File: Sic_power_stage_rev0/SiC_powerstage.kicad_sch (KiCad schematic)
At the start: 34 parts, among them Q10 NTBG014N120M3P, Q11 NTBG014N120M3P, Q12 NTBG014N120M3P, Q7 NTBG014N120M3P, Q8 NTBG014N120M3P, Q9 NTBG014N120M3P

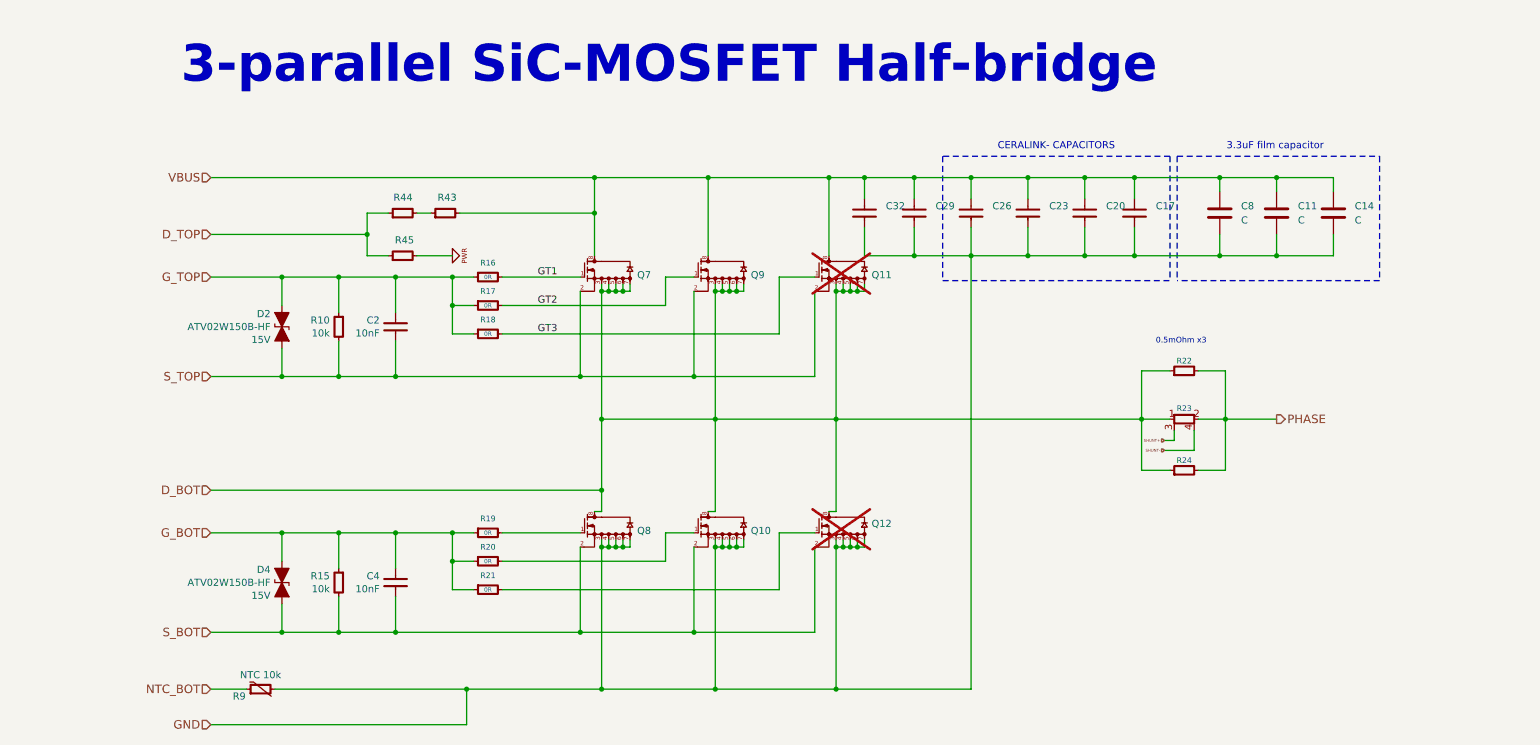
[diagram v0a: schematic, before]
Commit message: Increase clearance between mosfets, Add alternating film capacitor
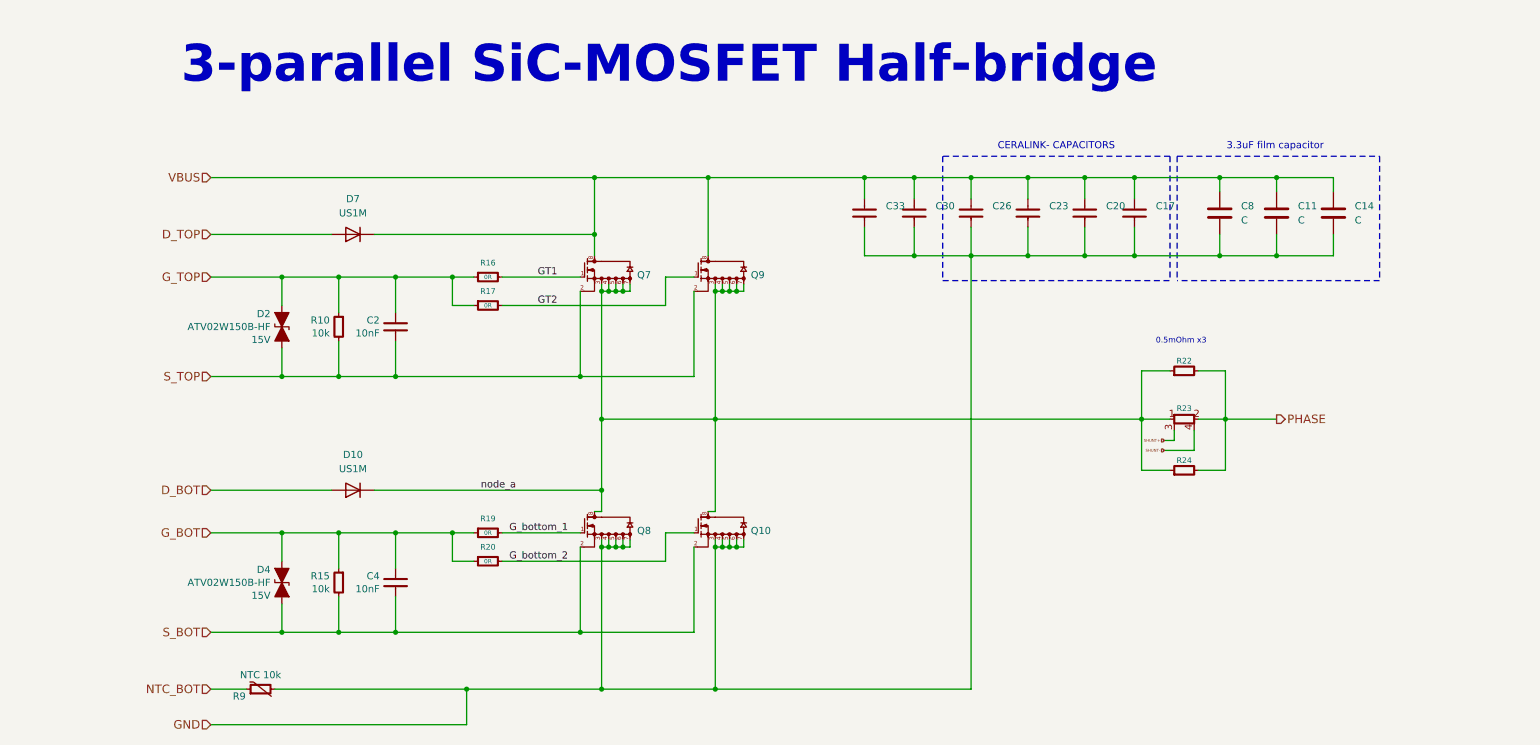
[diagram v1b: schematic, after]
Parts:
- removed Q11, Q12: NTBG014N120M3P, SiC_ONSEMI:D2PAK-7L, symbol SiC_ONSEMI:NTB6014N120M3P
- removed R18, R21: 0R, IPC7351-Nominal:RESC1608X50, symbol pasv-res:R-0603
- removed R43, R44, R45: R-1206, IPC7351-Nominal:RESC3216X60, symbol pasv-res:R-1206
- added D10, D7: US1M, Diode_SMD:D_SMA, symbol Diode:US1M
- renumbered C29 to C30, C32 to C33
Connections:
- net D_BOT: now also D10.2 (A); no longer Q10.8, Q7.3, Q7.4, Q7.5, Q7.6, Q7.7, Q8.8, Q9.3, Q9.4, Q9.5, Q9.6, Q9.7, R22.1, R23.1, R24.1
- net D_TOP: now also D7.2 (A)
- net VBUS: now also D7.1 (K)
- net G_bottom_2: now reaches Q10.1, R20.2
- net G_bottom_1: now reaches Q8.1, R19.2
- new net node_a: D10.1 (K), Q10.8, Q7.3, Q7.4, Q7.5, Q7.6, Q7.7, Q8.8, Q9.3, Q9.4, Q9.5, Q9.6, Q9.7, R22.1, R23.1, R24.1

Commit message: Move leg A to reduce Cu Area
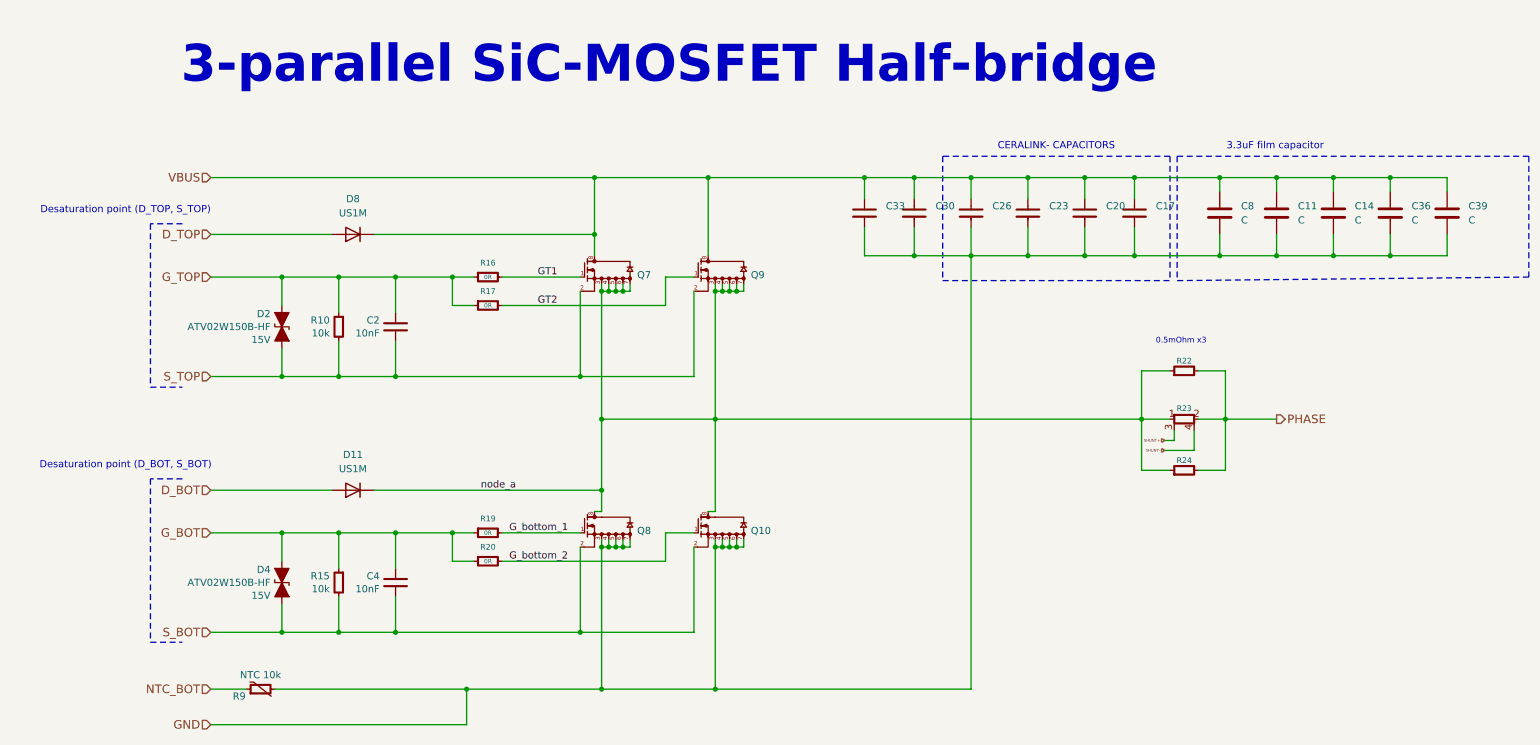
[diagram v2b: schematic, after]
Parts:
- added C36, C39: C, Capacitor_THT:C_Rect_L18.0mm_W9.0mm_P15.00mm_FKS3_FKP3, symbol Device:C
- renumbered D10 to D11, D7 to D8
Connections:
- net GND: now also C36.2, C39.2
- net VBUS: now also C36.1, C39.1
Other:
- note added: "Desaturation point (D_BOT, S_BOT)"
- note added: "Desaturation point (D_TOP, S_TOP)"

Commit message: Define Ceralink capacitor value and qty
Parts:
- C10: renamed from C11; value C -> 5uF; footprint Capacitor_THT:C_Rect_L18.0mm_W9.0mm_P15.00mm_FKS3_FKP3 -> Capacitor_THT:C_Rect_L31.5mm_W11.0mm_P27.50mm_MKS4; BOM (none) -> MKP DC FILTERING - 500VDC, 5UF 1; MFR (none) -> EPCOS - TDK Electronics; MPN (none) -> B32714H5505K000; Voltage (none) -> 500V
- C11: renamed from C14; value C -> 5uF; footprint Capacitor_THT:C_Rect_L18.0mm_W9.0mm_P15.00mm_FKS3_FKP3 -> Capacitor_THT:C_Rect_L31.5mm_W11.0mm_P27.50mm_MKS4; BOM (none) -> MKP DC FILTERING - 500VDC, 5UF 1; MFR (none) -> EPCOS - TDK Electronics; MPN (none) -> B32714H5505K000; Voltage (none) -> 500V
- C12: renamed from C36; value C -> 5uF; footprint Capacitor_THT:C_Rect_L18.0mm_W9.0mm_P15.00mm_FKS3_FKP3 -> Capacitor_THT:C_Rect_L31.5mm_W11.0mm_P27.50mm_MKS4; BOM (none) -> MKP DC FILTERING - 500VDC, 5UF 1; MFR (none) -> EPCOS - TDK Electronics; MPN (none) -> B32714H5505K000; Voltage (none) -> 500V
- C13: renamed from C39; value C -> 5uF; BOM (none) -> MKP DC FILTERING - 500VDC, 5UF 1; MFR (none) -> EPCOS - TDK Electronics; MPN (none) -> B32714H5505K000; Voltage (none) -> 500V
- C3: renamed from C33; value C-2220 -> 0.25uF; BOM (none) -> CERALINK SMD 2220 - 500 V; MFR (none) -> EPCOS - TDK Electronics; MPN (none) -> B58043I5254M052; Volatage (none) -> 500V
- C4: renamed from C30; value C-2220 -> 0.25uF; BOM (none) -> CERALINK SMD 2220 - 500 V; MFR (none) -> EPCOS - TDK Electronics; MPN (none) -> B58043I5254M052; Voltage (none) -> 500V
- C5: renamed from C26; value C-2220 -> 0.25uF; BOM (none) -> CERALINK SMD 2220 - 500 V; MFR (none) -> EPCOS - TDK Electronics; MPN (none) -> B58043I5254M052; Voltage (none) -> 500V
- C6: renamed from C23; value C-2220 -> 0.25uF; BOM (none) -> CERALINK SMD 2220 - 500 V; MFR (none) -> EPCOS - TDK Electronics; MPN (none) -> B58043I5254M052; Voltage (none) -> 500V
- C7: renamed from C20; value C-2220 -> 0.25uF; BOM (none) -> CERALINK SMD 2220 - 500 V; MFR (none) -> EPCOS - TDK Electronics; MPN (none) -> B58043I5254M052; Voltage (none) -> 500V
- C8: renamed from C17; value C-2220 -> 0.25uF; BOM (none) -> CERALINK SMD 2220 - 500 V; MFR (none) -> EPCOS - TDK Electronics; MPN (none) -> B58043I5254M052; Voltage (none) -> 500V
- C9: renamed from C8; value C -> 5uF; footprint Capacitor_THT:C_Rect_L18.0mm_W9.0mm_P15.00mm_FKS3_FKP3 -> Capacitor_THT:C_Rect_L31.5mm_W11.0mm_P27.50mm_MKS4; BOM (none) -> MKP DC FILTERING - 500VDC, 5UF 1; MFR (none) -> EPCOS - TDK Electronics; MPN (none) -> B32714H5505K000; Voltage (none) -> 500V
- Q1: renamed from Q7; footprint SiC_ONSEMI:D2PAK-7L -> Package_TO_SOT_SMD:TO-263-7_TabPin8; BOM (none) -> D2PAK7(TO-263-7L-HV) Silicon Carbide Field Effect Transisto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; LCSC Part # (none) -> C5209029; MFR (none) -> onsemi; MPN (none) -> NTBG014N120M3P
- Q2: renamed from Q8; footprint SiC_ONSEMI:D2PAK-7L -> Package_TO_SOT_SMD:TO-263-7_TabPin8; BOM (none) -> D2PAK7(TO-263-7L-HV) Silicon Carbide Field Effect Transisto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; LCSC Part # (none) -> C5209029; MFR (none) -> onsemi; MPN (none) -> NTBG014N120M3P
- Q3: renamed from Q9; footprint SiC_ONSEMI:D2PAK-7L -> Package_TO_SOT_SMD:TO-263-7_TabPin8; BOM (none) -> D2PAK7(TO-263-7L-HV) Silicon Carbide Field Effect Transisto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; LCSC Part # (none) -> C5209029; MFR (none) -> onsemi; MPN (none) -> NTBG014N120M3P
- Q4: renamed from Q10; footprint SiC_ONSEMI:D2PAK-7L -> Package_TO_SOT_SMD:TO-263-7_TabPin8; BOM (none) -> D2PAK7(TO-263-7L-HV) Silicon Carbide Field Effect Transisto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; LCSC Part # (none) -> C5209029; MFR (none) -> onsemi; MPN (none) -> NTBG014N120M3P
- renumbered C2 to C1, C4 to C2, D2 to D1, D4 to D2, D8 to D3, D11 to D4, R20 to R10, R22 to R11, R23 to R12, R24 to R13, R9 to R4, R10 to R5, R15 to R6, R16 to R7, R17 to R8, R19 to R9
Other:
- note added: "For 5uF rated 500v, rated size: 1.240" L x 0.433" W (31.50mm x 11.00mm)"
- note added: "SiC-MOSFET Half-bridge"
- note removed: "3-parallel SiC-MOSFET Half-bridge"
- moved on the sheet: C10, C11, C12, C13, C3, C5, C6, C7, C8, C9

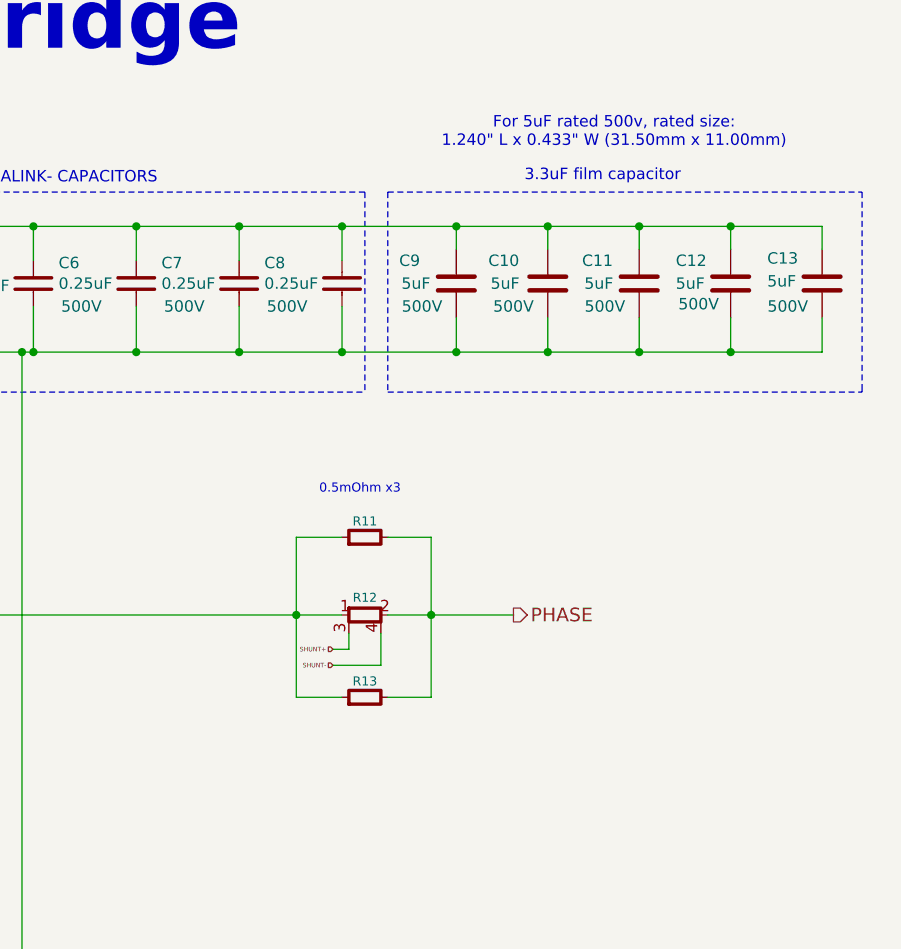
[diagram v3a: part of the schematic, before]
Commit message: Add changes
 - Add DC-LINK capacitor discharge circuit.
 - VBUS resistive divider.
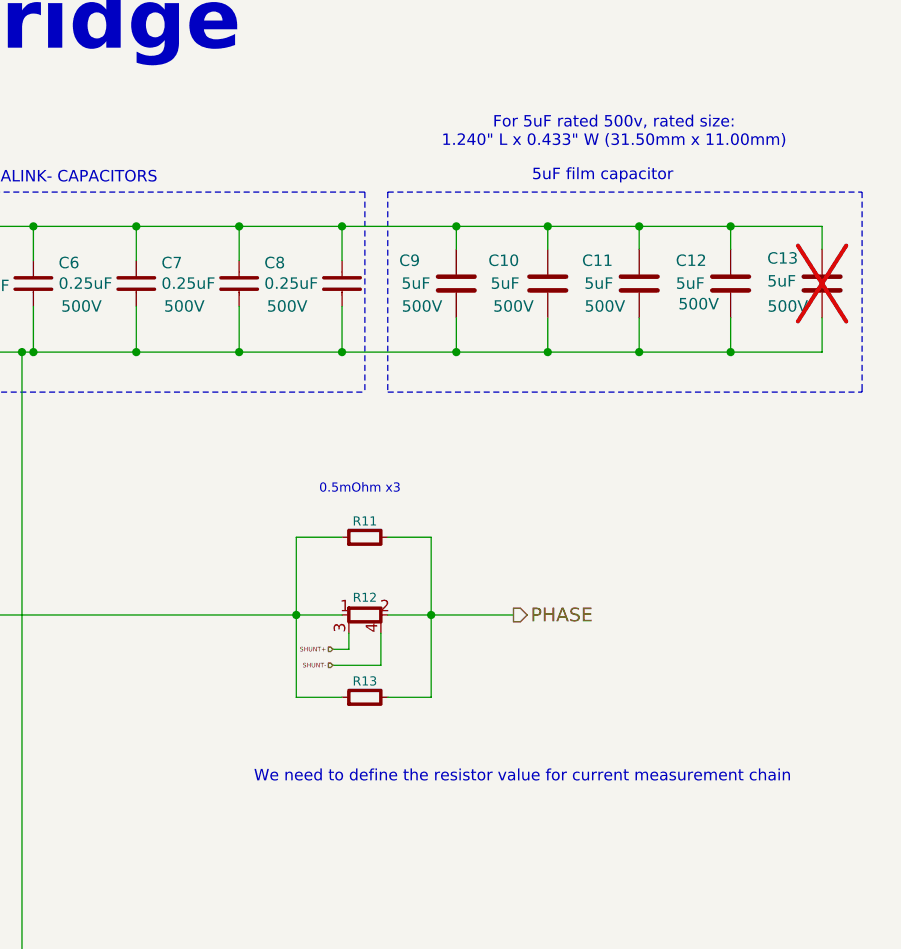
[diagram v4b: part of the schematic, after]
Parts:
- C13: now not fitted
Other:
- note added: "5uF film capacitor"
- note added: "We need to define the resistor value for current measurement chain"
- note removed: "3.3uF film capacitor"
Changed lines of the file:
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@@
 		)
 	)
+	(text "We need to define the resistor value for current measurement chain"
+		(exclude_from_sim no)
+		(at 235.966 109.474 0)
+		(effects
+			(font
+				(size 1.27 1.27)
+			)
+		)
+	)
 	(text "Desaturation point (D_TOP, S_TOP)\n"
 		(exclude_from_sim no)
@@
 		)
 	)
-	(text "3.3uF film capacitor\n"
+	(text "5uF film capacitor\n"
 		(exclude_from_sim no)
 		(at 244.856 42.672 0)
@@
 		(in_bom yes)
 		(on_board yes)
-		(dnp no)
+		(dnp yes)
 		(property "Reference" "C13"
 			(at 263.144 51.816 0)

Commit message: Add traces for leg A referring to gate and driver source
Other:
- note added: "Desaturation diode"
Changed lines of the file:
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@@
 	(generator_version "9.0")
 	(paper "A4")
+	(rectangle
+		(start 63.5 55.88)
+		(end 76.2 60.96)
+		(stroke
+			(width 0)
+			(type dash)
+		)
+		(fill
+			(type none)
+		)
+	)
 	(text "Desaturation point (D_BOT, S_BOT)\n"
 		(exclude_from_sim no)
@@
 		(effects
 			(font
+				(size 1.27 1.27)
+			)
+		)
+	)
+	(text "Desaturation diode\n"
+		(exclude_from_sim no)
+		(at 70.358 62.738 0)
+		(effects
+			(font
